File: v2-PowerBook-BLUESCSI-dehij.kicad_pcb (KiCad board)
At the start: 2 copper layers, 96.5 x 50.8 mm, 44 parts, among them J1 Micro_SD_Card, J2 Conn_02x20_Odd_Even, U1 YAAJ_BluePill_Part_Like

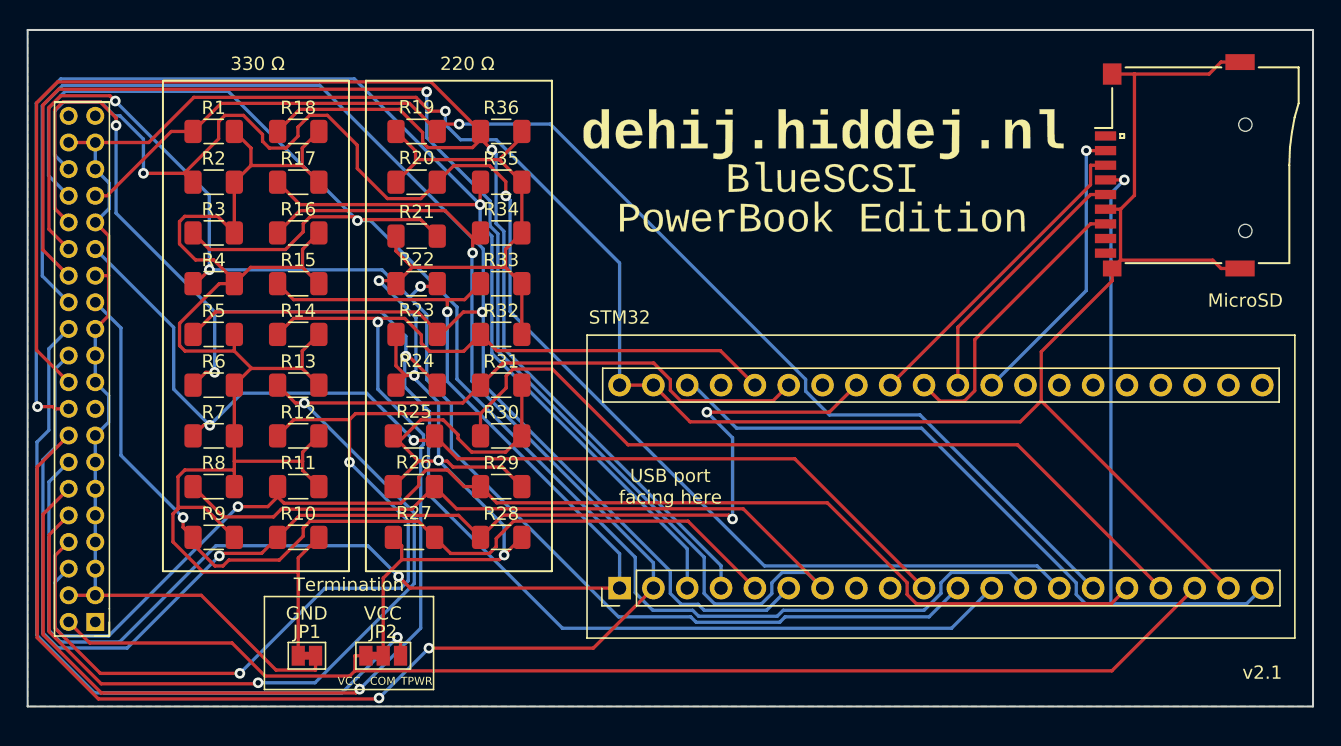
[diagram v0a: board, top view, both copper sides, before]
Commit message: Updated layout for JLCPCB assembly
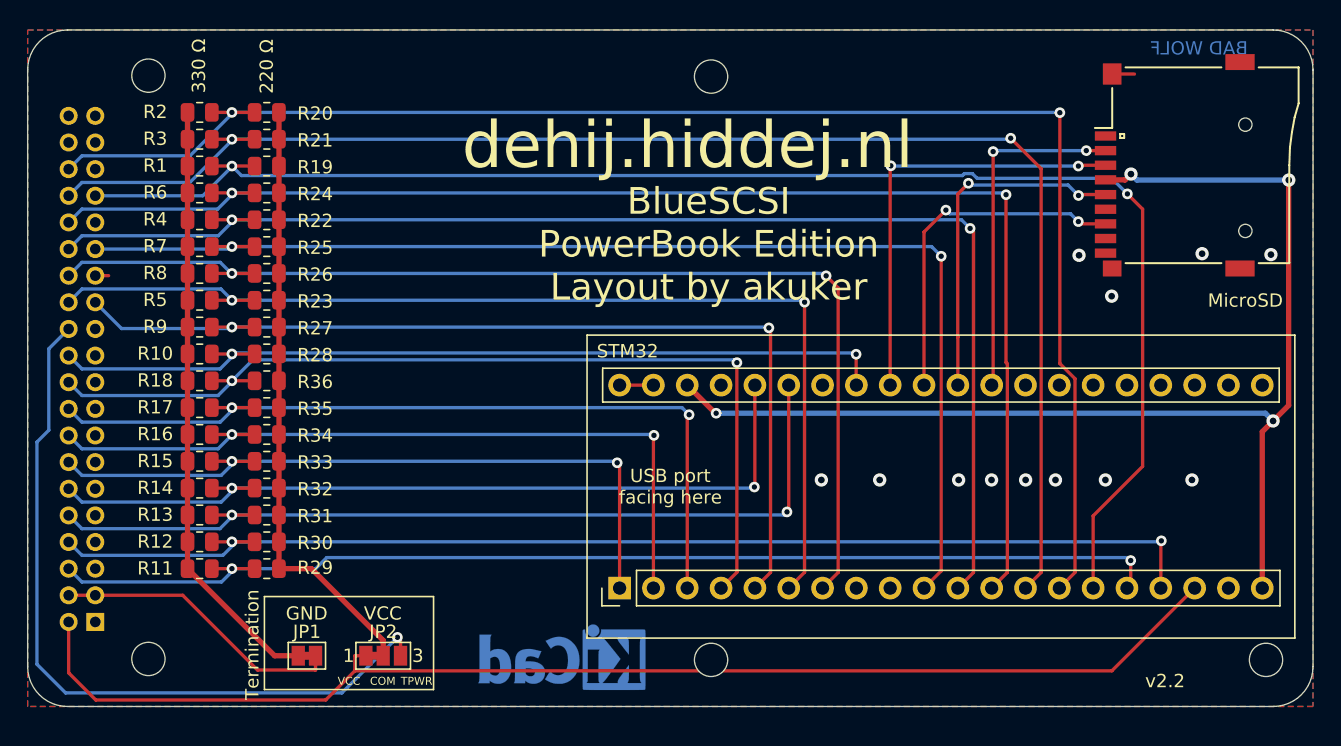
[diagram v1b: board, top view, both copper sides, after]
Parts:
- removed G1: LOGO, Other footprints:Backsilkscreen
- removed G2: LOGO, Other footprints:PBlogo2
- removed the REF** at (85.1, 120.7)
- added H1: MountingHole, MountingHole:MountingHole_2.5mm, F.Cu at (82.7, 79.6)
- added H2: MountingHole, MountingHole:MountingHole_2.5mm, F.Cu at (125.0, 79.7)
- added H3: MountingHole, MountingHole:MountingHole_2.5mm, F.Cu at (82.7, 123.4)
- added H4: MountingHole, MountingHole:MountingHole_2.5mm, F.Cu at (125.0, 123.5)
- added H5: MountingHole, MountingHole:MountingHole_2.5mm, F.Cu at (166.7, 123.5)
- added REF**: KiCad-Logo_5mm_Copper, Symbol:KiCad-Logo_5mm_Copper, B.Cu at (113.8, 123.8)
- R1, R10, R11, R12, R13, R14, R15, R16, R17, R18, R2, R3, R4, R5, R6, R7, R8, R9: value R -> 330; footprint Resistor_SMD:R_1206_3216Metric_Pad1.30x1.75mm_HandSolder -> Resistor_SMD:R_0805_2012Metric
- R19, R20, R21, R22, R23, R24, R25, R26, R27, R28, R29, R30, R31, R32, R33, R34, R35, R36: value R -> 220; footprint Resistor_SMD:R_1206_3216Metric_Pad1.30x1.75mm_HandSolder -> Resistor_SMD:R_0805_2012Metric
- moved R36 25.7 mm to (91.6, 102.5)
- moved R35 24.4 mm to (91.6, 104.6)
- moved R34 23.2 mm to (91.6, 106.6)
- moved R28 22.3 mm to (91.6, 100.5)
- moved R33 22.1 mm to (91.6, 108.6)
- moved R32 21.1 mm to (91.6, 110.6)
- moved R18 20.1 mm to (86.6, 102.5), turned to 0 degrees
- moved R31 20.1 mm to (91.6, 112.6)
- moved R26 19.4 mm to (91.6, 94.5), turned to 180 degrees
- moved R30 19.3 mm to (91.6, 114.6)
- moved R27 19.3 mm to (91.6, 98.5), turned to 180 degrees
- moved R29 18.6 mm to (91.6, 116.7)
- moved R17 18.5 mm to (86.6, 104.6), turned to 0 degrees
- moved R24 18.3 mm to (91.6, 88.4), turned to 180 degrees
- moved R25 18.0 mm to (91.6, 92.5), turned to 180 degrees
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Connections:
- J1 pad 1: Net-(J1-Pad1) -> unconnected-(J1-Pad1)
- J1 pad 8: Net-(J1-Pad8) -> unconnected-(J1-Pad8)
- J1 pad 9: Net-(J1-Pad9) -> GND
- J2 pad 1: Net-(J2-Pad1) -> unconnected-(J2-Pad1)
- J2 pad 17: Net-(J2-Pad17) -> unconnected-(J2-Pad17)
- J2 pad 39: Net-(J2-Pad39) -> unconnected-(J2-Pad39)
- J2 pad 40: Net-(J2-Pad40) -> unconnected-(J2-Pad40)
- U1 pad 21: Net-(U1-Pad21) -> unconnected-(U1-Pad21)
- U1 pad 22: Net-(U1-Pad22) -> unconnected-(U1-Pad22)
- U1 pad 23: Net-(U1-Pad23) -> unconnected-(U1-Pad23)
- U1 pad 24: Net-(U1-Pad24) -> unconnected-(U1-Pad24)
- U1 pad 25: Net-(U1-Pad25) -> unconnected-(U1-Pad25)
- U1 pad 26: Net-(U1-Pad26) -> unconnected-(U1-Pad26)
- U1 pad 27: Net-(U1-Pad27) -> unconnected-(U1-Pad27)
- U1 pad 28: Net-(U1-Pad28) -> unconnected-(U1-Pad28)
- U1 pad 34: Net-(U1-Pad34) -> unconnected-(U1-Pad34)
- U1 pad 37: Net-(U1-Pad37) -> unconnected-(U1-Pad37)
- U1 pad 8: Net-(U1-Pad8) -> unconnected-(U1-Pad8)
- U1 pad 9: Net-(U1-Pad9) -> unconnected-(U1-Pad9)
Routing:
- net GND: track 218.3 -> 26.6 mm, vias 1 -> 12
- net Net-(JP2-Pad2): track 120.4 -> 45.5 mm, vias 4 -> 0
- net Net-(JP1-Pad1): track 116.7 -> 45.3 mm
- net /SCSI_ACK: track 152.8 -> 85.4 mm, vias 1 -> 2
- net /SCSI_DAT5: track 116.7 -> 59.6 mm, vias 3 -> 2
- net /SCSI_DAT6: track 116.1 -> 64.0 mm
- net /SCSI_DAT4: track 104.0 -> 54.8 mm
- net /SCSI_DAT3: track 108.5 -> 63.2 mm
- net /SCSI_DAT7: track 117.1 -> 72.4 mm, vias 1 -> 2
- net /SCSI_DAT1: track 129.0 -> 89.8 mm
- net /SCSI_BSY: track 120.1 -> 81.3 mm, vias 1 -> 2
- net /SCSI_DBP: track 100.4 -> 65.6 mm, vias 3 -> 2
- net /SCSI_DAT2: track 100.8 -> 67.7 mm
- net /SCSI_IO: track 94.0 -> 114.3 mm, vias 1 -> 2
- net /SCSI_CD: track 125.4 -> 111.0 mm, vias 1 -> 2
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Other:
- outline, holes or cut-outs redrawn
- board text added: "09-2022"
- board text added: "BAD WOLF"
- board text added: "BlueSCSI PowerBook Edition Layout by akuker"
- board text added: "dehij.hiddej.nl"
- board text added: "v2.2"
- board text removed: "01-2022"
- board text removed: "v2.1"
